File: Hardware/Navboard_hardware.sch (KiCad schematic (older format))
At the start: 13 parts

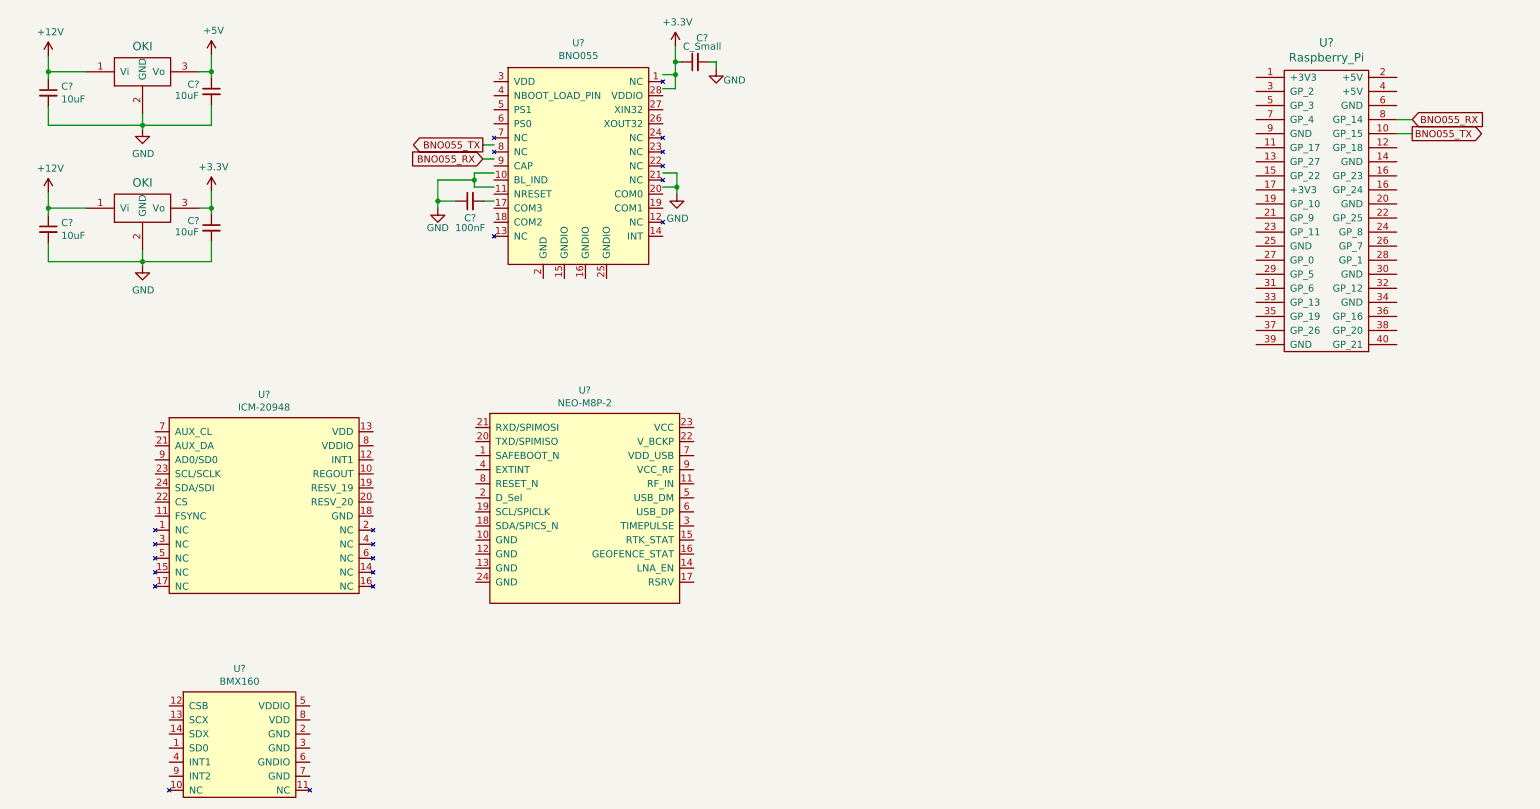
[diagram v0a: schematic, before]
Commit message: Completed the schematic for the IMUs but still need to add indicators and have a schematic review.
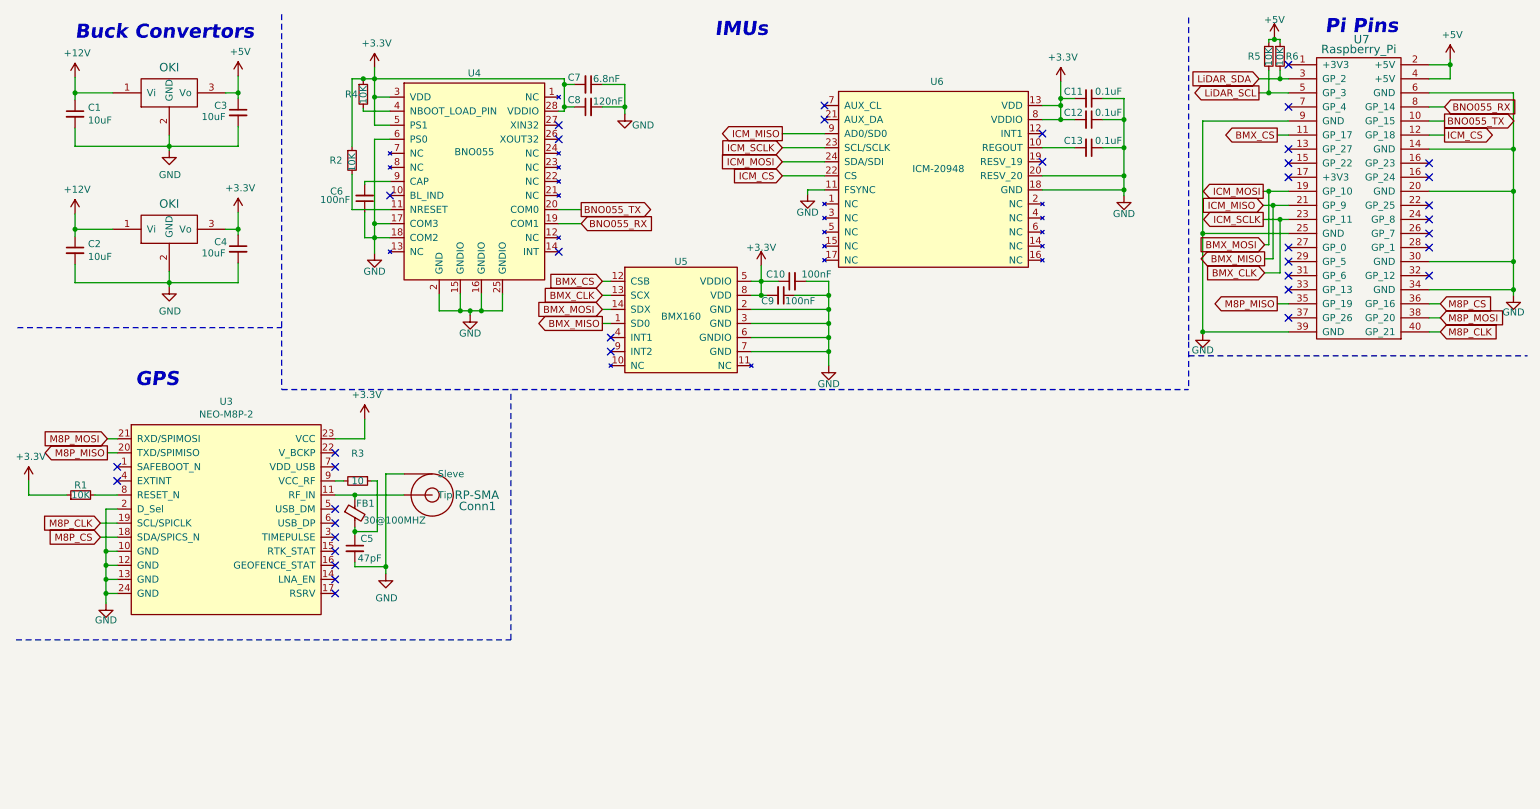
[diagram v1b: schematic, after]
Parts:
- added C10, C9: 100nF, symbol Device:C_Small
- added C11, C12, C13: 0.1uF, symbol Device:C_Small
- added C5: 47pF, symbol Device:C_Small
- added C7: 6.8nF, symbol Device:C_Small
- added Conn1: RP-SMA, symbol MRDT_Connectors:RP-SMA
- added FB1: 30@100MHZ, symbol Device:FerriteBead_Small
- added R1, R2, R4, R5, R6: 10K, symbol Device:R_Small
- added R3: 10, symbol Device:R_Small
- C8: renamed from C?; value C_Small -> 120nF
- gave numbers to parts that had none: 12
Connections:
- net labels added: BMX_CLK, BMX_CS, BMX_MISO, BMX_MOSI, ICM_CS, ICM_MISO, ICM_MOSI, ICM_SCLK, LiDAR_SCL, LiDAR_SDA, M8P_CLK, M8P_CS, M8P_MISO, M8P_MOSI
- wire segments 49 -> 199
- no-connect marks 0 -> 38
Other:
- note added: "Buck Convertors"
- note added: "GPS"
- note added: "IMUs"
- note added: "Pi Pins"
- moved on the sheet: C1, C2, C3, C4, C6, C8, U3, U4, U5, U6, U7

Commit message: Finished Layout but needs review
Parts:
- added Conn?: LiDAR, symbol MRDT_Connectors:Molex_SL_04
- added D? (x2): GREEN, symbol Device:LED_Small
- added D? (x13): BLUE, symbol Device:LED_Small
- added R? (x14): 520, symbol Device:R_Small
- added R?: 330, symbol Device:R_Small
- FB1: value 30@100MHZ -> 30@100MHZ/2.0A
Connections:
- net +3V3: now also R?.1
- net +5V: now also Conn?.1, R?.1
- net BMX_CS: now also R?.1
- net BMX_MISO: now also R?.1, R?.1
- net BMX_MOSI: now also R?.1, R?.1
- net BNO055_RX: now also R?.1
- net BNO055_TX: now also R?.1
- net GND: now also Conn?.2, D?.1 (K), D?.1 (K), D?.1 (K), D?.1 (K), D?.1 (K), D?.1 (K), D?.1 (K), D?.1 (K), D?.1 (K), D?.1 (K), D?.1 (K), D?.1 (K), D?.1 (K), D?.1 (K), D?.1 (K)
- net ICM_CS: now also R?.1
- net LiDAR_SCL: now also Conn?.4, R?.1
- net LiDAR_SDA: now also Conn?.3, R?.1
- net M8P_CS: now also R?.1
- net M8P_MISO: now also R?.1
- net M8P_MOSI: now also R?.1
- new net: D?.2 (A), R?.2 (x15)
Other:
- note added: "Indicators"
- note added: "LiDAR"

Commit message: Added footprints
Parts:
- C1, C10, C11, C12, C13, C2, C3, C4, C5, C6, C7, C8, C9: footprint (none) -> Capacitor_SMD:C_0603_1608Metric_Pad1.08x0.95mm_HandSolder
- Conn1: footprint (none) -> MRDT_Connectors:RP-SMA_Jack_Tru-Hole_Right-Angle
- Conn2: renamed from Conn?; footprint (none) -> MRDT_Connectors:MOLEX_SL_04_Horizontal
- D1, D10, D11, D12, D13, D14, D15, D2, D3, D4, D5, D6, D7, D8, D9: renamed from D?; footprint (none) -> LED_SMD:LED_0603_1608Metric_Pad1.05x0.95mm_HandSolder
- FB1, R1, R2, R3, R4, R5, R6: footprint (none) -> Resistor_SMD:R_0603_1608Metric_Pad0.98x0.95mm_HandSolder
- R10, R11, R12, R13, R14, R15, R16, R17, R18, R19, R20, R21, R7, R8, R9: renamed from R?; footprint (none) -> Resistor_SMD:R_0603_1608Metric_Pad0.98x0.95mm_HandSolder
- U1: value OKI -> OKI-5V; footprint (none) -> MRDT_Devices:OKI_Horizontal
- U2: value OKI -> OKI-3V; footprint (none) -> MRDT_Devices:OKI_Horizontal
- U7: footprint (none) -> MRDT_Shields:RaspberryPi_THT_BOTTOM

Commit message: Started Layout
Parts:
- added Conn3: AndersonPP, MRDT_Connectors:Anderson_2_Horizontal_Side_by_Side, symbol MRDT_Connectors:AndersonPP
- added D16, D17, D18, D19: GREEN, LED_SMD:LED_0603_1608Metric_Pad1.05x0.95mm_HandSolder, symbol Device:LED_Small
- added R22, R23, R24, R25: 330, Resistor_SMD:R_0603_1608Metric_Pad0.98x0.95mm_HandSolder, symbol Device:R_Small
- U4: footprint MRDT_ICs:LGA28R50P4X10_380X520X100 -> MRDT_ICs:BNO055
- U5: footprint MRDT_ICs:PQFN50P250X300X100-14N -> MRDT_ICs:BMX160
- U6: footprint MRDT_ICs:QFN40P300X300X105-24N -> MRDT_ICs:ICM_20948
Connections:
- net +12V: now also Conn3.2 (V+Log)
- net +3V3: now also R22.1, R23.1, R24.1, R25.1
- net GND: now also Conn3.1 (GND), D16.1 (K), D17.1 (K), D18.1 (K), D19.1 (K)
- new net: D16.2 (A), R22.2
- new net: D17.2 (A), R23.2
- new net: D18.2 (A), R24.2
- new net: D19.2 (A), R25.2
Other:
- note added: "Power"
- note removed: "Buck Convertors"
- moved on the sheet: C1, C2, C3, C4, Conn2

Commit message: Layout almost finished just need to complete LED traces.
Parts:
- removed D16, D17, D18, D19: GREEN, LED_SMD:LED_0603_1608Metric_Pad1.05x0.95mm_HandSolder, symbol Device:LED_Small
- removed R22, R23, R24, R25: 330, Resistor_SMD:R_0603_1608Metric_Pad0.98x0.95mm_HandSolder, symbol Device:R_Small
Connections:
- net LiDAR_SCL: now also Conn2.3; no longer Conn2.4
- net LiDAR_SDA: now also Conn2.4; no longer Conn2.3
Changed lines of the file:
@@
 $EndComp
-Wire Wire Line
-	3130 1060 3020 1060
 Wire Wire Line
 	3020 930  4370 930
@@
 Wire Wire Line
 	2860 1860 2860 1610
-Wire Wire Line
-	3020 850  3020 930
 Connection ~ 2940 930
 Wire Wire Line
@@
 Wire Wire Line
 	7900 1220 7770 1220
-Wire Wire Line
-	7770 1120 7900 1120
 Connection ~ 7900 1120
 Wire Wire Line
@@
 L power:+3.3V #PWR0115
 U 1 1 600A5685
-P 5770 2180
-F 0 "#PWR0115" H 5770 2030 50  0001 C CNN
-F 1 "+3.3V" H 5770 2310 50  0000 C CNN
-F 2 "" H 5770 2180 50  0001 C CNN
-F 3 "" H 5770 2180 50  0001 C CNN
-	1    5770 2180
+P 5750 2180
+F 0 "#PWR0115" H 5750 2030 50  0001 C CNN
+F 1 "+3.3V" H 5750 2310 50  0000 C CNN
+F 2 "" H 5750 2180 50  0001 C CNN
+F 3 "" H 5750 2180 50  0001 C CNN
+	1    5750 2180
 	1    0    0    -1
 $EndComp
@@
 	0    -1   -1   0
 $EndComp
-Wire Wire Line
-	5770 2470 5700 2470
-Wire Wire Line
-	5700 2370 5770 2370
-Connection ~ 5770 2370
-Wire Wire Line
-	5770 2370 5770 2470
-Wire Wire Line
-	5770 2470 5810 2470
-Connection ~ 5770 2470
-Wire Wire Line
-	5770 2370 5890 2370
 Wire Wire Line
 	6010 2470 6250 2470
@@
 Wire Wire Line
 	2950 3490 2950 3350
-Wire Wire Line
-	2740 3490 2950 3490
 $Comp
 L power:+3.3V #PWR0122
@@
 	1    0    0    -1
 $EndComp
-Text GLabel 10410 5070 0    50   Input ~ 0
+Text GLabel 10410 5170 0    50   Input ~ 0
 LiDAR_SDA
-Text GLabel 10410 5170 0    50   Output ~ 0
+Text GLabel 10410 5070 0    50   Output ~ 0
 LiDAR_SCL
 $Comp
@@
 Wire Wire Line
 	10460 5170 10410 5170
-Text GLabel 8010 910  2    50   Output ~ 0
-ICM_ON
-Wire Wire Line
-	8010 910  7900 910
-Wire Wire Line
-	7900 910  7900 1070
-Wire Wire Line
-	7900 910  7900 850
-Connection ~ 7900 910
-Text GLabel 3110 850  2    50   Output ~ 0
-BNO_ON
-Wire Wire Line
-	3020 850  3110 850
-Wire Wire Line
-	3020 850  3020 800
-Connection ~ 3020 850
-Text GLabel 5810 2220 2    50   Output ~ 0
-BMX_ON
-Wire Wire Line
-	5810 2220 5770 2220
-Wire Wire Line
-	5770 2220 5770 2370
-Wire Wire Line
-	5770 2220 5770 2180
-Connection ~ 5770 2220
-Text GLabel 3030 3490 2    50   Output ~ 0
-M8P_ON
-Wire Wire Line
-	2950 3490 3030 3490
-Connection ~ 2950 3490
-$Comp
-L Device:LED_Small D16
-U 1 1 609FEC29
-P 9180 4150
-F 0 "D16" V 9260 4300 50  0000 R CNN
-F 1 "GREEN" V 9180 4100 50  0000 R CNN
-F 2 "LED_SMD:LED_0603_1608Metric_Pad1.05x0.95mm_HandSolder" V 9180 4150 50  0001 C CNN
-F 3 "~" V 9180 4150 50  0001 C CNN
-	1    9180 4150
-	0    -1   -1   0
-$EndComp
-$Comp
-L power:GND #PWR020
-U 1 1 609FEC2F
-P 9180 4300
-F 0 "#PWR020" H 9180 4050 50  0001 C CNN
-F 1 "GND" H 9180 4180 50  0000 C CNN
-F 2 "" H 9180 4300 50  0001 C CNN
-F 3 "" H 9180 4300 50  0001 C CNN
-	1    9180 4300
-	1    0    0    -1
-$EndComp
-$Comp
-L Device:R_Small R22
-U 1 1 609FEC35
-P 9180 3900
-F 0 "R22" H 9040 3900 50  0000 L CNN
-F 1 "330" V 9180 3830 50  0000 L CNN
-F 2 "Resistor_SMD:R_0603_1608Metric_Pad0.98x0.95mm_HandSolder" H 9180 3900 50  0001 C CNN
-F 3 "~" H 9180 3900 50  0001 C CNN
-	1    9180 3900
-	1    0    0    -1
-$EndComp
-Wire Wire Line
-	9180 3740 9180 3800
-Wire Wire Line
-	9180 4000 9180 4050
-Wire Wire Line
-	9180 4250 9180 4300
-$Comp
-L Device:LED_Small D17
-U 1 1 609FEC3F
-P 9560 4150
-F 0 "D17" V 9640 4310 50  0000 R CNN
-F 1 "GREEN" V 9560 4100 50  0000 R CNN
-F 2 "LED_SMD:LED_0603_1608Metric_Pad1.05x0.95mm_HandSolder" V 9560 4150 50  0001 C CNN
-F 3 "~" V 9560 4150 50  0001 C CNN
-	1    9560 4150
-	0    -1   -1   0
-$EndComp
-$Comp
-L power:GND #PWR021
-U 1 1 609FEC45
-P 9560 4300
-F 0 "#PWR021" H 9560 4050 50  0001 C CNN
-F 1 "GND" H 9560 4180 50  0000 C CNN
-F 2 "" H 9560 4300 50  0001 C CNN
-F 3 "" H 9560 4300 50  0001 C CNN
-	1    9560 4300
-	1    0    0    -1
-$EndComp
-$Comp
-L Device:R_Small R23
-U 1 1 609FEC4B
-P 9560 3900
-F 0 "R23" H 9420 3900 50  0000 L CNN
-F 1 "330" V 9560 3830 50  0000 L CNN
-F 2 "Resistor_SMD:R_0603_1608Metric_Pad0.98x0.95mm_HandSolder" H 9560 3900 50  0001 C CNN
-F 3 "~" H 9560 3900 50  0001 C CNN
-	1    9560 3900
-	1    0    0    -1
-$EndComp
-Wire Wire Line
-	9560 3800 9560 3740
-Wire Wire Line
-	9560 4000 9560 4050
-Wire Wire Line
-	9560 4250 9560 4300
-$Comp
-L Device:LED_Small D18
-U 1 1 609FEC55
-P 9940 4150
-F 0 "D18" V 10020 4310 50  0000 R CNN
-F 1 "GREEN" V 9940 4100 50  0000 R CNN
-F 2 "LED_SMD:LED_0603_1608Metric_Pad1.05x0.95mm_HandSolder" V 9940 4150 50  0001 C CNN
-F 3 "~" V 9940 4150 50  0001 C CNN
-	1    9940 4150
-	0    -1   -1   0
-$EndComp
-$Comp
-L power:GND #PWR022
-U 1 1 609FEC5B
-P 9940 4300
-F 0 "#PWR022" H 9940 4050 50  0001 C CNN
-F 1 "GND" H 9940 4180 50  0000 C CNN
-F 2 "" H 9940 4300 50  0001 C CNN
-F 3 "" H 9940 4300 50  0001 C CNN
-	1    9940 4300
-	1    0    0    -1
-$EndComp
-$Comp
-L Device:R_Small R24
-U 1 1 609FEC61
-P 9940 3900
-F 0 "R24" H 9760 3900 50  0000 L CNN
-F 1 "330" V 9940 3830 50  0000 L CNN
-F 2 "Resistor_SMD:R_0603_1608Metric_Pad0.98x0.95mm_HandSolder" H 9940 3900 50  0001 C CNN
-F 3 "~" H 9940 3900 50  0001 C CNN
-	1    9940 3900
-	1    0    0    -1
-$EndComp
-Wire Wire Line
-	9940 3800 9940 3740
-Wire Wire Line
-	9940 4000 9940 4050
-Wire Wire Line
-	9940 4250 9940 4300
-$Comp
-L Device:LED_Small D19
-U 1 1 609FEC6B
-P 10320 4150
-F 0 "D19" V 10400 4310 50  0000 R CNN
-F 1 "GREEN" V 10320 4100 50  0000 R CNN
-F 2 "LED_SMD:LED_0603_1608Metric_Pad1.05x0.95mm_HandSolder" V 10320 4150 50  0001 C CNN
-F 3 "~" V 10320 4150 50  0001 C CNN
-	1    10320 4150
-	0    -1   -1   0
-$EndComp
-$Comp
-L power:GND #PWR023
-U 1 1 609FEC71
-P 10320 4300
-F 0 "#PWR023" H 10320 4050 50  0001 C CNN
-F 1 "GND" H 10320 4180 50  0000 C CNN
-F 2 "" H 10320 4300 50  0001 C CNN
-F 3 "" H 10320 4300 50  0001 C CNN
-	1    10320 4300
-	1    0    0    -1
-$EndComp
-$Comp
-L Device:R_Small R25
-U 1 1 609FEC77
-P 10320 3900
-F 0 "R25" H 10140 3900 50  0000 L CNN
-F 1 "330" V 10320 3830 50  0000 L CNN
-F 2 "Resistor_SMD:R_0603_1608Metric_Pad0.98x0.95mm_HandSolder" H 10320 3900 50  0001 C CNN
-F 3 "~" H 10320 3900 50  0001 C CNN
-	1    10320 3900
-	1    0    0    -1
-$EndComp
-Wire Wire Line
-	10320 3800 10320 3740
-Wire Wire Line
-	10320 4000 10320 4050
-Wire Wire Line
-	10320 4250 10320 4300
-Text GLabel 9560 3740 1    50   Input ~ 0
-ICM_ON
-Text GLabel 9180 3740 1    50   Input ~ 0
-M8P_ON
-Text GLabel 9940 3740 1    50   Input ~ 0
-BMX_ON
-Text GLabel 10320 3740 1    50   Input ~ 0
-BNO_ON
 Wire Notes Line
 	3990 4480 11220 4480
@@
 Wire Wire Line
 	10520 2730 10600 2730
+Wire Wire Line
+	3020 800  3020 930
+Wire Wire Line
+	5700 2470 5750 2470
+Wire Wire Line
+	5750 2180 5750 2370
+Connection ~ 5750 2470
+Wire Wire Line
+	5750 2470 5810 2470
+Wire Wire Line
+	5700 2370 5750 2370
+Wire Wire Line
+	7900 850  7900 1070
+Connection ~ 5750 2370
+Wire Wire Line
+	5750 2370 5890 2370
+Wire Wire Line
+	5750 2370 5750 2470
+Wire Wire Line
+	3020 1060 3130 1060
+Wire Wire Line
+	7770 1120 7900 1120
+Wire Wire Line
+	2740 3490 2950 3490
 $EndSCHEMATC

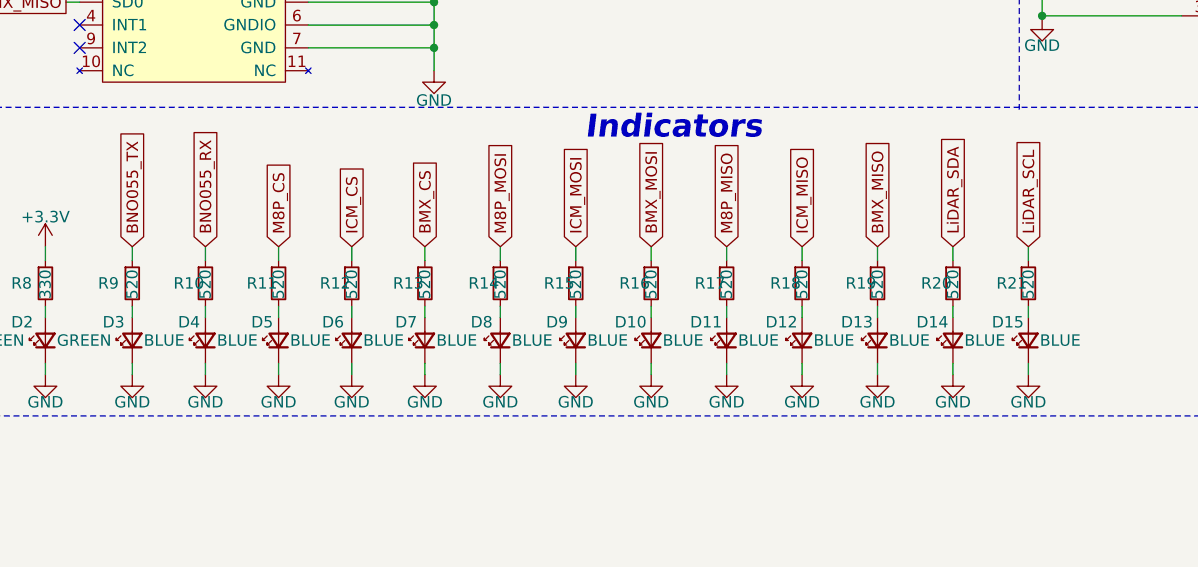
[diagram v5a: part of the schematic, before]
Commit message: Finished Layout but I still need to complete the BOM and generate GERBs.
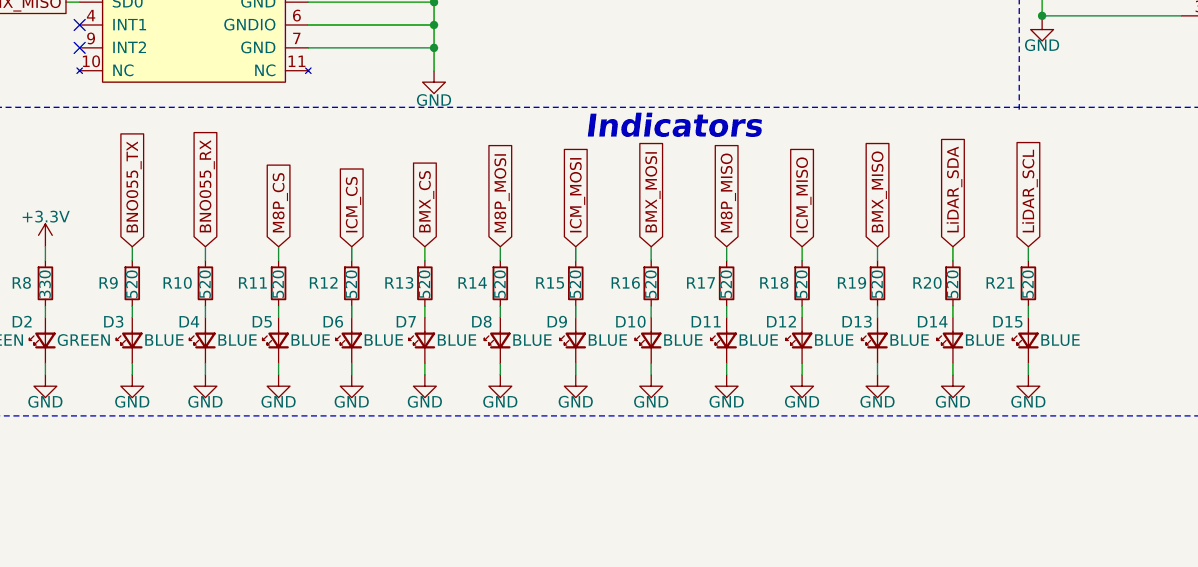
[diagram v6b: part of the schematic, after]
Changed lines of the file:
@@
 U 1 1 605A4623
 P 5570 3900
-F 0 "R11" H 5430 3900 50  0000 L CNN
+F 0 "R11" H 5390 3900 50  0000 L CNN
 F 1 "520" V 5570 3830 50  0000 L CNN
 F 2 "Resistor_SMD:R_0603_1608Metric_Pad0.98x0.95mm_HandSolder" H 5570 3900 50  0001 C CNN
@@
 U 1 1 605A4852
 P 5890 3900
-F 0 "R12" H 5750 3900 50  0000 L CNN
+F 0 "R12" H 5700 3900 50  0000 L CNN
 F 1 "520" V 5890 3830 50  0000 L CNN
 F 2 "Resistor_SMD:R_0603_1608Metric_Pad0.98x0.95mm_HandSolder" H 5890 3900 50  0001 C CNN
@@
 U 1 1 605A4435
 P 5250 3900
-F 0 "R10" H 5110 3900 50  0000 L CNN
+F 0 "R10" H 5060 3900 50  0000 L CNN
 F 1 "520" V 5250 3830 50  0000 L CNN
 F 2 "Resistor_SMD:R_0603_1608Metric_Pad0.98x0.95mm_HandSolder" H 5250 3900 50  0001 C CNN
@@
 U 1 1 6069DEAE
 P 6210 3900
-F 0 "R13" H 6070 3900 50  0000 L CNN
+F 0 "R13" H 6030 3900 50  0000 L CNN
 F 1 "520" V 6210 3830 50  0000 L CNN
 F 2 "Resistor_SMD:R_0603_1608Metric_Pad0.98x0.95mm_HandSolder" H 6210 3900 50  0001 C CNN
@@
 U 1 1 606C775F
 P 6540 3900
-F 0 "R14" H 6400 3900 50  0000 L CNN
+F 0 "R14" H 6350 3900 50  0000 L CNN
 F 1 "520" V 6540 3830 50  0000 L CNN
 F 2 "Resistor_SMD:R_0603_1608Metric_Pad0.98x0.95mm_HandSolder" H 6540 3900 50  0001 C CNN
@@
 U 1 1 60701678
 P 6870 3900
-F 0 "R15" H 6730 3900 50  0000 L CNN
+F 0 "R15" H 6690 3900 50  0000 L CNN
 F 1 "520" V 6870 3830 50  0000 L CNN
 F 2 "Resistor_SMD:R_0603_1608Metric_Pad0.98x0.95mm_HandSolder" H 6870 3900 50  0001 C CNN
@@
 U 1 1 6072D3AF
 P 7200 3900
-F 0 "R16" H 7060 3900 50  0000 L CNN
+F 0 "R16" H 7020 3900 50  0000 L CNN
 F 1 "520" V 7200 3830 50  0000 L CNN
 F 2 "Resistor_SMD:R_0603_1608Metric_Pad0.98x0.95mm_HandSolder" H 7200 3900 50  0001 C CNN
@@
 U 1 1 60768D30
 P 7530 3900
-F 0 "R17" H 7390 3900 50  0000 L CNN
+F 0 "R17" H 7350 3900 50  0000 L CNN
 F 1 "520" V 7530 3830 50  0000 L CNN
 F 2 "Resistor_SMD:R_0603_1608Metric_Pad0.98x0.95mm_HandSolder" H 7530 3900 50  0001 C CNN
@@
 U 1 1 60796EAD
 P 7860 3900
-F 0 "R18" H 7720 3900 50  0000 L CNN
+F 0 "R18" H 7670 3900 50  0000 L CNN
 F 1 "520" V 7860 3830 50  0000 L CNN
 F 2 "Resistor_SMD:R_0603_1608Metric_Pad0.98x0.95mm_HandSolder" H 7860 3900 50  0001 C CNN
@@
 U 1 1 607D73E7
 P 8190 3900
-F 0 "R19" H 8050 3900 50  0000 L CNN
+F 0 "R19" H 8010 3900 50  0000 L CNN
 F 1 "520" V 8190 3830 50  0000 L CNN
 F 2 "Resistor_SMD:R_0603_1608Metric_Pad0.98x0.95mm_HandSolder" H 8190 3900 50  0001 C CNN
@@
 U 1 1 60807728
 P 8520 3900
-F 0 "R20" H 8380 3900 50  0000 L CNN
+F 0 "R20" H 8340 3900 50  0000 L CNN
 F 1 "520" V 8520 3830 50  0000 L CNN
 F 2 "Resistor_SMD:R_0603_1608Metric_Pad0.98x0.95mm_HandSolder" H 8520 3900 50  0001 C CNN
@@
 U 1 1 608E8B40
 P 8850 3900
-F 0 "R21" H 8710 3900 50  0000 L CNN
+F 0 "R21" H 8660 3900 50  0000 L CNN
 F 1 "520" V 8850 3830 50  0000 L CNN
 F 2 "Resistor_SMD:R_0603_1608Metric_Pad0.98x0.95mm_HandSolder" H 8850 3900 50  0001 C CNN
